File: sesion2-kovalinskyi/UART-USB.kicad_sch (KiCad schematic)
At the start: 5 parts, among them J3 USB_C_Receptacle_USB2.0_16P, U6 CH340C

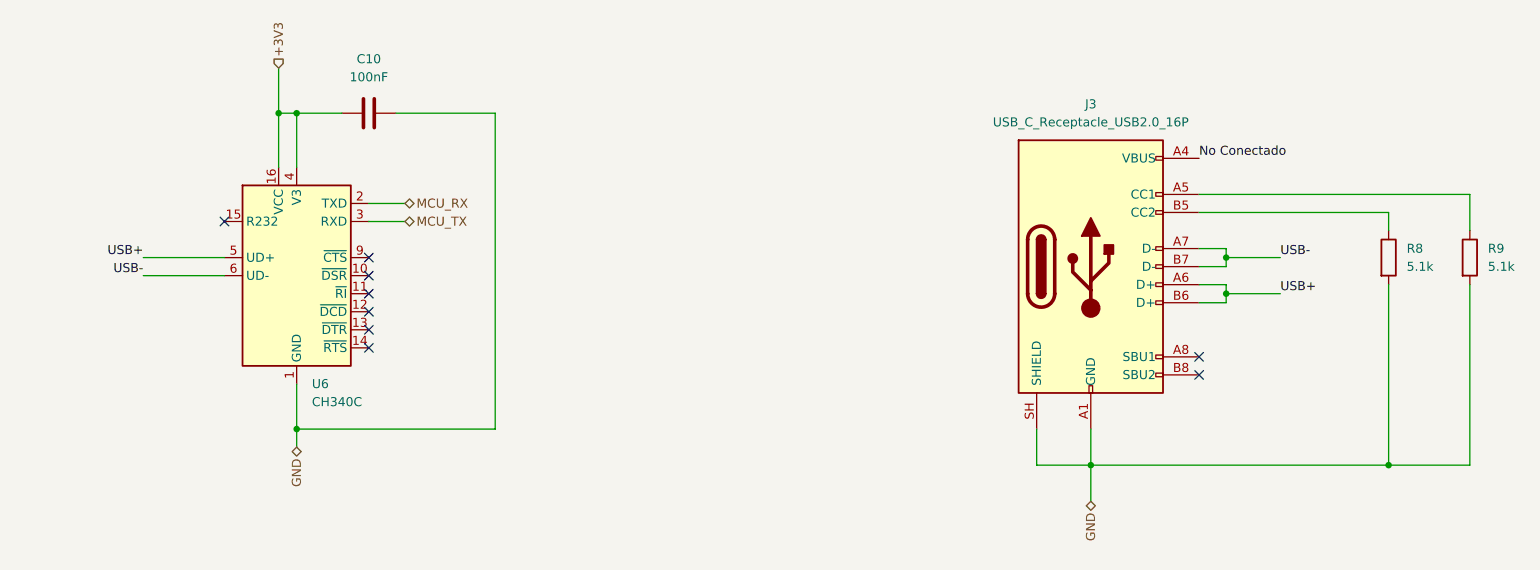
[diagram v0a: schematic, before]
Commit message: Apartados 1 - 3 completados; integrando protecciones (apartado 4) en el esquemático
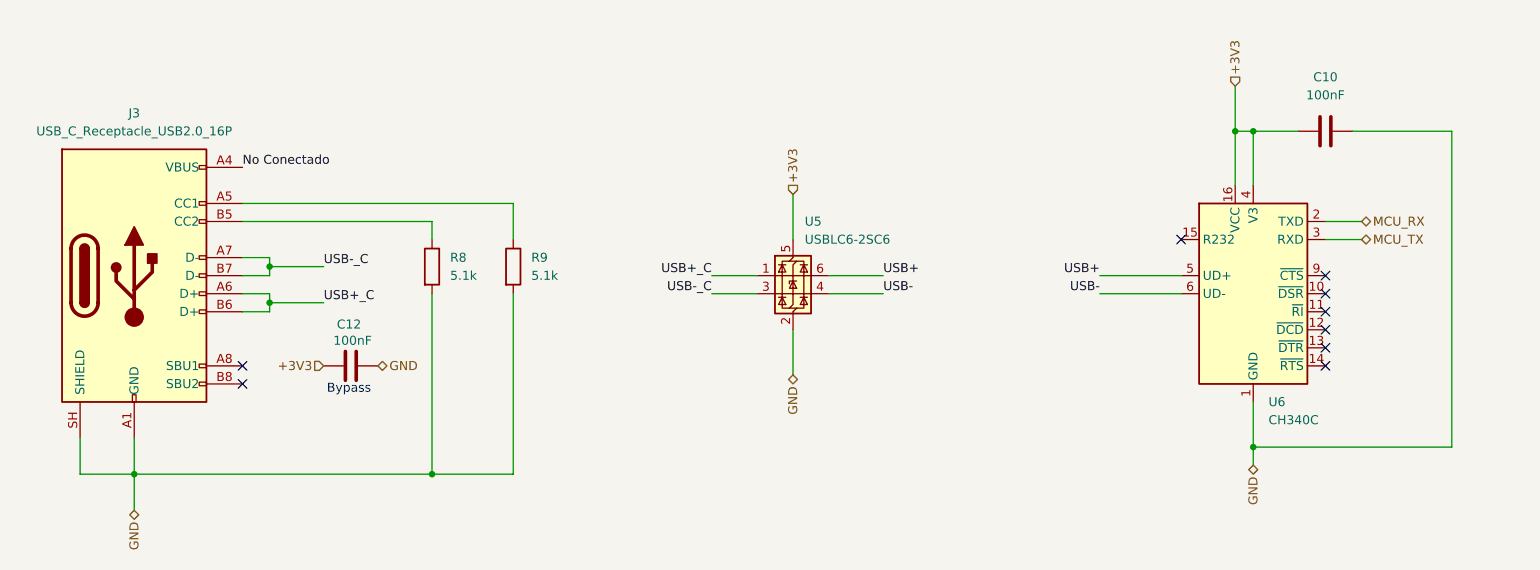
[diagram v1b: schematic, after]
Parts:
- added C12: 100nF, Capacitor_SMD:C_0805_2012Metric, symbol Device:C
- added U5: USBLC6-2SC6, Package_TO_SOT_SMD:SOT-23-6, symbol Power_Protection:USBLC6-2SC6
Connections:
- net +3V3: now also C12.1, U5.5 (VBUS)
- net GND: now also C12.2, U5.2 (GND)
- net USB+: now also U5.6 (I/O1); no longer J3.A6 (D+), J3.B6 (D+)
- net USB-: now also U5.4 (I/O2); no longer J3.A7 (D-), J3.B7 (D-)
- new net USB+_C: J3.A6 (D+), J3.B6 (D+), U5.1 (I/O1)
- new net USB-_C: J3.A7 (D-), J3.B7 (D-), U5.3 (I/O2)
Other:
- note added: "Bypass"
- moved on the sheet: C10, J3, R8, R9, U6

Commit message: Copia de seguridad Sesión 5
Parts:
- C10, C12: MPN (none) -> CC0805KRX7R9BB104
- J3: MPN (none) -> TYPE-C-31-M-12
- R8, R9: MPN (none) -> RC0805FR-075K1L
- U5: MPN (none) -> USBLC6-2SC6
- U6: MPN (none) -> CH340C
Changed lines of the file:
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@@
+			)
+		)
+		(property "MPN" "TYPE-C-31-M-12"
+			(at 55.88 86.36 0)
+			(hide yes)
+			(show_name no)
+			(do_not_autoplace no)
+			(effects
+				(font
+					(size 1.27 1.27)
+				)
 			)
 		)
@@
 			)
 		)
+		(property "MPN" "CC0805KRX7R9BB104"
+			(at 223.52 66.04 90)
+			(hide yes)
+			(show_name no)
+			(do_not_autoplace no)
+			(effects
+				(font
+					(size 1.27 1.27)
+				)
+			)
+		)
 		(pin "1"
 		)
@@
 		(property "Description" "Unpolarized capacitor"
 			(at 86.36 99.06 0)
+			(hide yes)
+			(show_name no)
+			(do_not_autoplace no)
+			(effects
+				(font
+					(size 1.27 1.27)
+				)
+			)
+		)
+		(property "MPN" "CC0805KRX7R9BB104"
+			(at 86.36 99.06 90)
 			(hide yes)
 			(show_name no)
@@
 			)
 		)
+		(property "MPN" "USBLC6-2SC6"
+			(at 148.59 86.36 0)
+			(hide yes)
+			(show_name no)
+			(do_not_autoplace no)
+			(effects
+				(font
+					(size 1.27 1.27)
+				)
+			)
+		)
 		(pin "1"
 		)
@@
 		)
 		(property "Description" "Resistor"
+			(at 97.79 85.09 0)
+			(hide yes)
+			(show_name no)
+			(do_not_autoplace no)
+			(effects
+				(font
+					(size 1.27 1.27)
+				)
+			)
+		)
+		(property "MPN" "RC0805FR-075K1L"
 			(at 97.79 85.09 0)
 			(hide yes)
@@
 			)
 		)
+		(property "MPN" "CH340C"
+			(at 213.36 88.9 0)
+			(hide yes)
+			(show_name no)
+			(do_not_autoplace no)
+			(effects
+				(font
+					(size 1.27 1.27)
+				)
+			)
+		)
 		(pin "12"
 		)
@@
 			(at 109.22 85.09 0)
 			(hide yes)
+			(show_name no)
+			(do_not_autoplace no)
+			(effects
+				(font
+					(size 1.27 1.27)
+				)
+			)
+		)
+		(property "MPN" "RC0805FR-075K1L"
+			(at 109.22 85.09 0)
+			(hide yes)

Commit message: Sesión 5 - LAYOUT FINAL (verificar Vías de Cosido)
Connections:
- net USB+_C renamed C_USB+
- net USB-_C renamed C_USB-
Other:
- moved on the sheet: C12
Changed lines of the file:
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@@
 	(text "Bypass"
 		(exclude_from_sim no)
-		(at 86.106 102.362 0)
+		(at 86.106 106.172 0)
 		(effects
 			(font
@@
 		)
 	)
-	(label "USB-_C"
+	(label "C_USB-"
 		(at 137.16 88.9 180)
 		(effects
@@
 		)
 	)
-	(label "USB+_C"
+	(label "C_USB+"
 		(at 82.55 90.17 0)
 		(effects
@@
 		)
 	)
-	(label "USB-_C"
+	(label "C_USB-"
 		(at 82.55 85.09 0)
 		(effects
@@
 		)
 	)
-	(label "USB+_C"
+	(label "C_USB+"
 		(at 137.16 86.36 180)
 		(effects
@@
 	(hierarchical_label "+3V3"
 		(shape input)
-		(at 82.55 99.06 180)
+		(at 82.55 102.87 180)
 		(effects
 			(font
@@
 	(hierarchical_label "GND"
 		(shape bidirectional)
-		(at 90.17 99.06 0)
+		(at 90.17 102.87 0)
 		(effects
 			(font
@@
 		(length 2.54)
 		(shape round)
-		(at 73.66 83.82 0)
-		(fields_autoplaced yes)
+		(at 77.47 85.09 0)
 		(effects
 			(font
@@
 		)
 		(property "Netclass" "DIFF_90"
-			(at 74.3585 81.28 0)
+			(at 78.1685 82.55 0)
 			(show_name no)
 			(do_not_autoplace no)
@@
 		)
 		(property "Component Class" ""
-			(at 40.64 8.89 0)
+			(at 44.45 10.16 0)
 			(show_name no)
 			(do_not_autoplace no)
@@
 		(length 2.54)
 		(shape round)
-		(at 73.66 91.44 180)
+		(at 77.47 90.17 180)
 		(fields_autoplaced yes)
 		(effects
@@
 		)
 		(property "Netclass" "DIFF_90"
-			(at 74.3585 93.98 0)
+			(at 78.1685 92.71 0)
 			(show_name no)
 			(do_not_autoplace no)
@@
 		)
 		(property "Component Class" ""
-			(at 40.64 16.51 0)
+			(at 44.45 15.24 0)
 			(show_name no)
 			(do_not_autoplace no)
@@
 	(symbol
 		(lib_id "Device:C")
-		(at 86.36 99.06 90)
+		(at 86.36 102.87 90)
 		(unit 1)
 		(body_style 1)
@@
 		(dnp no)
 		(property "Reference" "C12"
-			(at 86.106 93.218 90)
+			(at 86.106 97.028 90)
 			(show_name no)
 			(do_not_autoplace no)
@@
 		)
 		(property "Value" "100nF"
-			(at 86.614 95.504 90)
+			(at 86.614 99.314 90)
 			(show_name no)
 			(do_not_autoplace no)
@@
 		)
 		(property "Footprint" "Capacitor_SMD:C_0805_2012Metric"
-			(at 90.17 98.0948 0)
+			(at 90.17 101.9048 0)
 			(hide yes)
 			(show_name no)
@@
 		)
 		(property "Datasheet" ""
-			(at 86.36 99.06 0)
+			(at 86.36 102.87 0)
 			(hide yes)
 			(show_name no)
@@
 		)
 		(property "Description" "Unpolarized capacitor"
-			(at 86.36 99.06 0)
+			(at 86.36 102.87 0)
 			(hide yes)
 			(show_name no)
@@
 		)
 		(property "MPN" "CC0805KRX7R9BB104"
-			(at 86.36 99.06 90)
-			(hide yes)
-			(show_name no)
+			(at 86.36 102.87 90)
+			(hide yes)
+			(show_name no)
